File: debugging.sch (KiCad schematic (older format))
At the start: 1 part, among them X0 Arduino_Mega2560_Shield

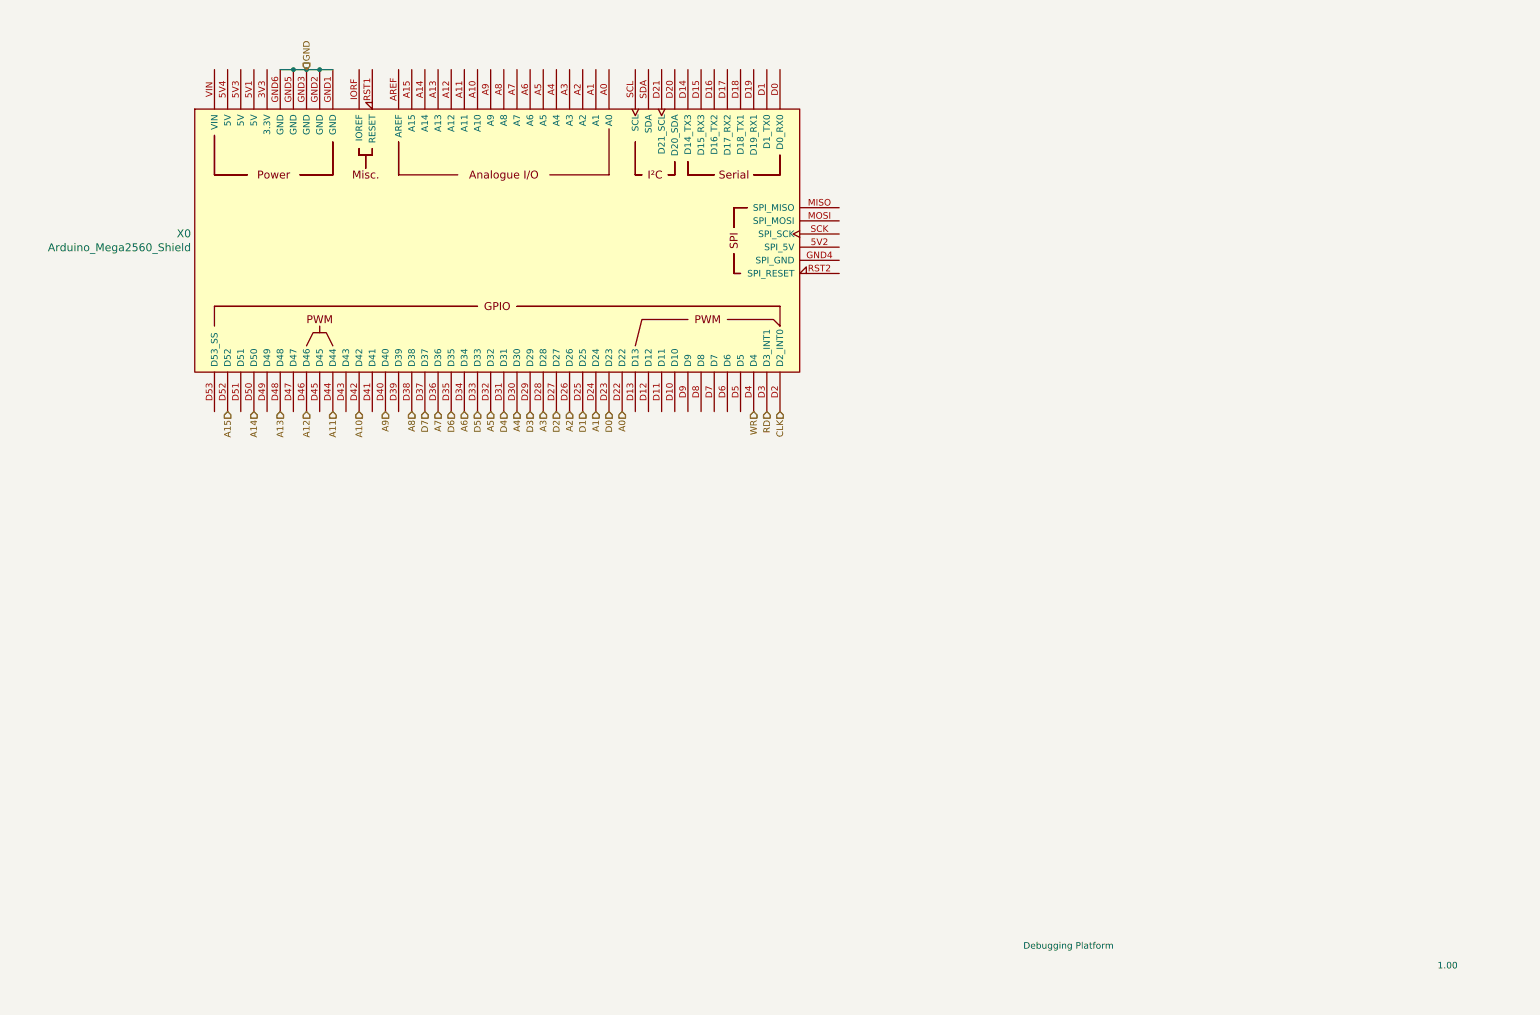
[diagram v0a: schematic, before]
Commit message: added additional schematics for submodules of the computer, So far just debugging module and the i/o expansion module
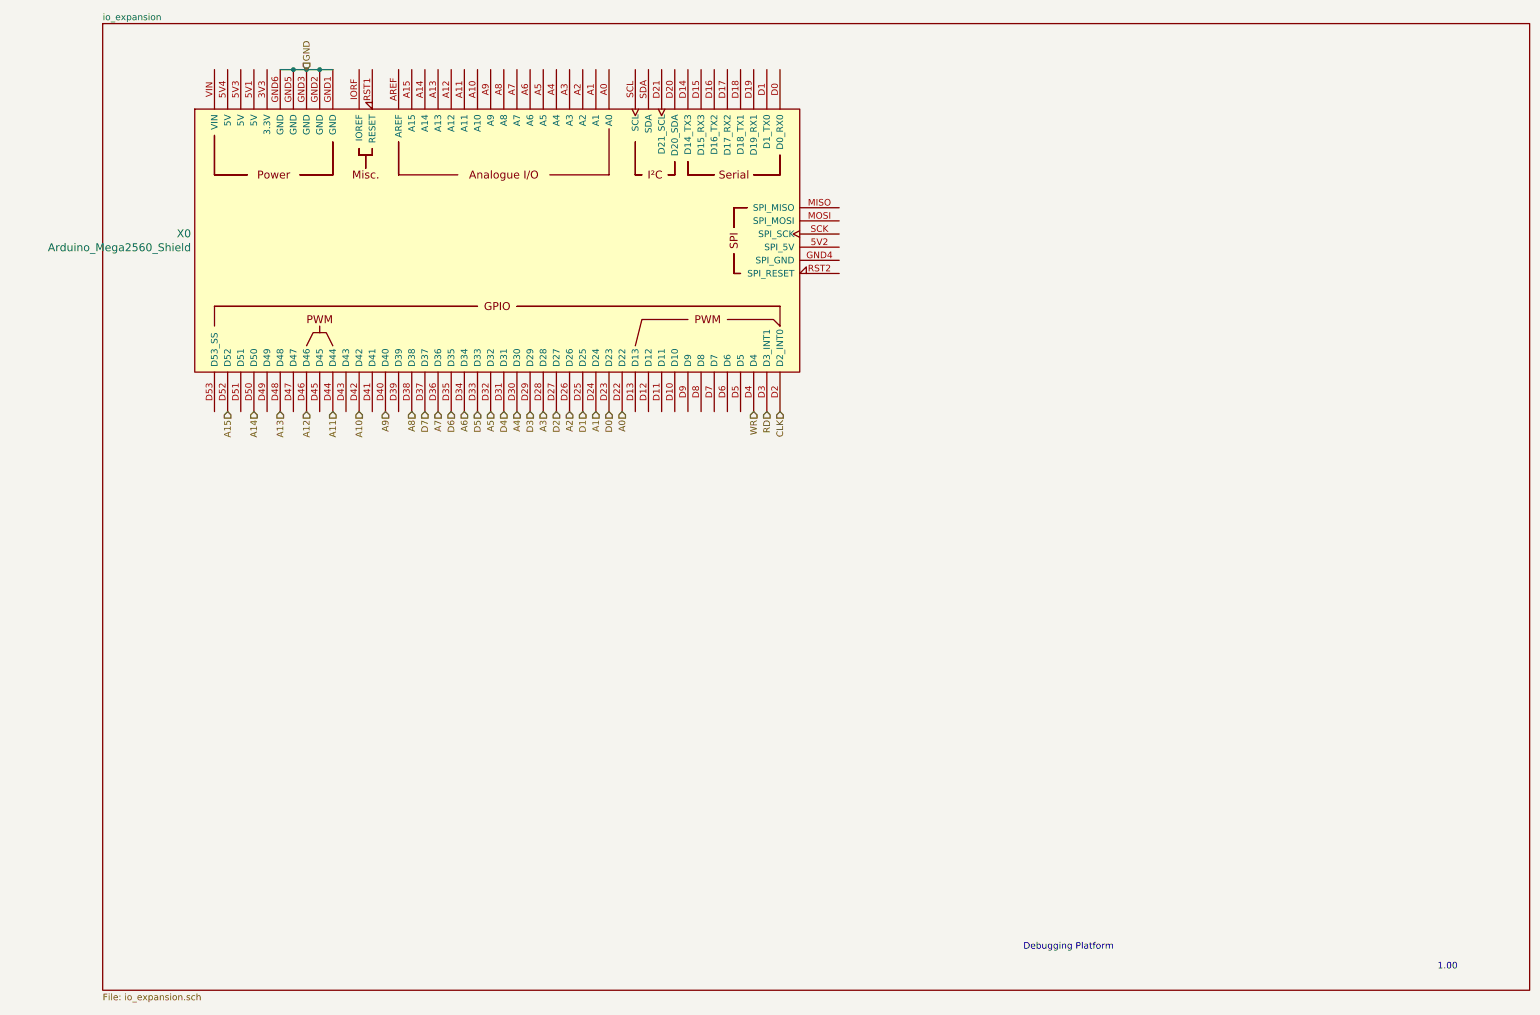
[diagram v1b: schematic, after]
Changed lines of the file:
@@
 $Descr A4 11693 8268
 encoding utf-8
-Sheet 2 2
+Sheet 2 3
 Title ""
 Date ""
@@
 Text Notes 10600 7650 0    50   ~ 0
 1.00
+$Sheet
+S 450  450  10850 7350
+U 5F638FE5
+F0 "io_expansion" 50
+F1 "io_expansion.sch" 50
+$EndSheet
 $EndSCHEMATC
